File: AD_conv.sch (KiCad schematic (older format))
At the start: 30 parts, among them U9 74AHCT244

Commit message: 8-way buffer for ADC changed to 74ACT244PW second attempt
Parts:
- removed U9: 74AHCT244, symbol 74xx:74AHCT244
- added U9: 74ACT244PW, symbol OpenVent:74ACT244PW
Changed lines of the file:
@@
 $EndDescr
-$Comp
-L 74xx:74AHCT244 U9
-U 1 1 601B9EB9
-P 2650 2300
-F 0 "U9" H 2800 3100 50  0000 C CNN
-F 1 "74AHCT244" H 2950 3000 50  0000 C CNN
-F 2 "" H 2650 2300 50  0001 C CNN
-F 3 "https://assets.nexperia.com/documents/data-sheet/74AHC_AHCT244.pdf" H 2650 2300 50  0001 C CNN
-	1    2650 2300
-	1    0    0    -1
-$EndComp
 $Comp
 L OpenVent:100K_0603_Chip_Resistor,_1%,_0.1W R73
@@
 Wire Wire Line
 	4750 900  4950 900
+$Comp
+L OpenVent:74ACT244PW U9
+U 1 1 6054710B
+P 2650 2300
+F 0 "U9" H 2350 3100 50  0000 C CNN
+F 1 "74ACT244PW" H 2300 3000 50  0000 C CNN
+F 2 "" H 2650 2300 50  0001 C CNN
+F 3 "https://drive.google.com/drive/u/1/folders/1bT0MezjjDfDXdTdQktjf6O5y5oTJs8ND" H 2650 2300 50  0001 C CNN
+	1    2650 2300
+	1    0    0    -1
+$EndComp
 $EndSCHEMATC

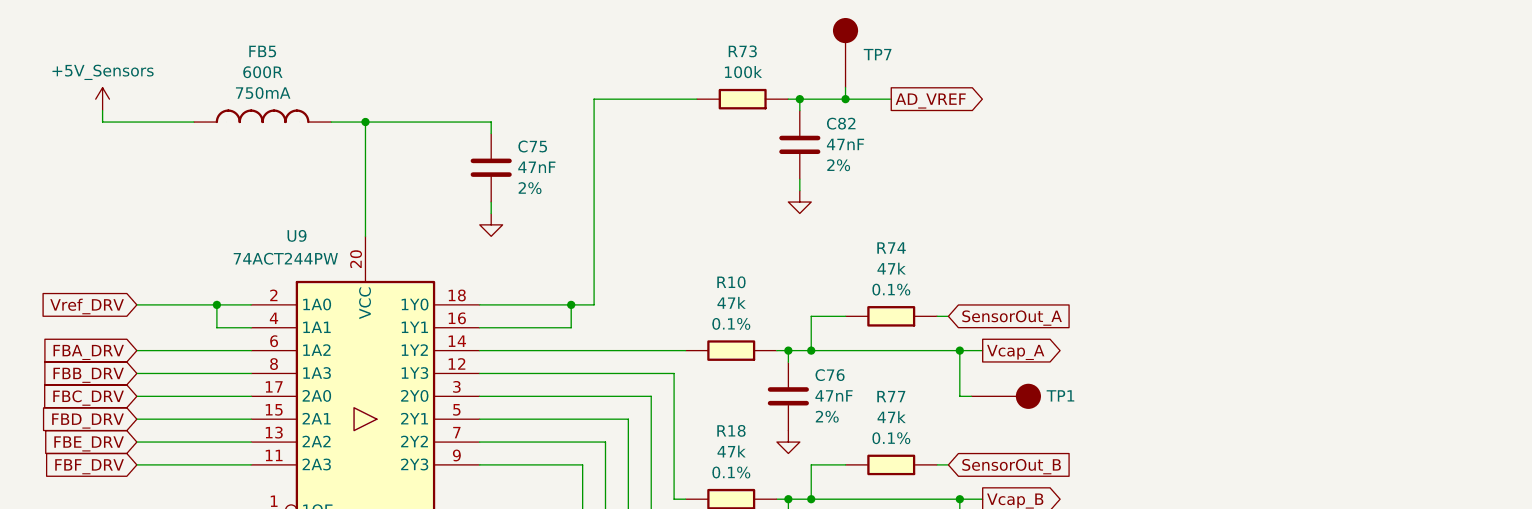
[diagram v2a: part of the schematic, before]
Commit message: Removed second Vref from U9 on ADC page, replaced with additional 8th input, G
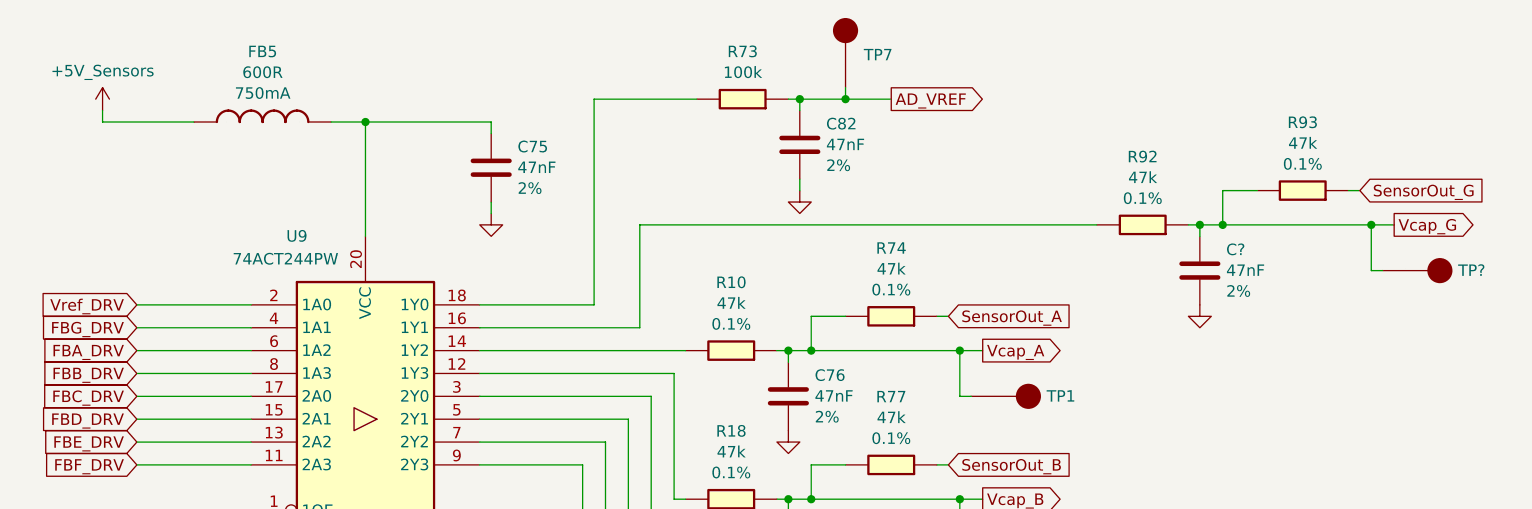
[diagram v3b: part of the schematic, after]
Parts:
- added C?: C_1206_47nF_16V_2%_PPS_film, Capacitor_SMD:C_1206_3216Metric, symbol OpenVent:C_1206_47nF_16V_2%_PPS_film
- added R92, R93: R_0603_47K_0.1%_0.1W_Film, Resistor_SMD:R_0603_1608Metric_Pad0.98x0.95mm_HandSolder, symbol OpenVent:R_0603_47K_0.1%_0.1W_Film
- added TP?: Test_Point_PTH, symbol OpenVent:Test_Point_PTH
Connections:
- net GND: now also C?.2
- net Vref_DRV: no longer U9.4 (1A1)
- net at R73.2, U9.18 (1Y0): no longer U9.16 (1Y1)
- new net: R92.2, U9.16 (1Y1)
- new net FBG_DRV: U9.4 (1A1)
- new net SensorOut_G: R93.1
- new net Vcap_G: C?.1, R92.1, R93.2, TP?.1
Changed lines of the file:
@@
 Text GLabel 1650 1800 0    50   Input ~ 0
 Vref_DRV
-Wire Wire Line
-	2150 1800 2000 1800
-Wire Wire Line
-	2150 1900 2000 1900
-Wire Wire Line
-	2000 1900 2000 1800
-Connection ~ 2000 1800
-Wire Wire Line
-	2000 1800 1650 1800
 Text GLabel 1650 2000 0    50   Input ~ 0
 FBA_DRV
@@
 $EndComp
 Wire Wire Line
-	3150 1800 3550 1800
-Wire Wire Line
 	3650 1800 3650 900
 Wire Wire Line
 	3650 900  4100 900
-Wire Wire Line
-	3150 1900 3550 1900
-Wire Wire Line
-	3550 1900 3550 1800
-Connection ~ 3550 1800
-Wire Wire Line
-	3550 1800 3650 1800
 Wire Wire Line
 	4500 900  4550 900
@@
 	1    0    0    -1
 $EndComp
+Wire Wire Line
+	1650 1800 2150 1800
+Wire Wire Line
+	3150 1800 3650 1800
+Text GLabel 1650 1900 0    50   Input ~ 0
+FBG_DRV
+Wire Wire Line
+	1650 1900 2150 1900
+$Comp
+L OpenVent:R_0603_47K_0.1%_0.1W_Film R92
+U 1 1 60565157
+P 6150 1550
+F 0 "R92" H 6250 1153 50  0000 C CNN
+F 1 "R_0603_47K_0.1%_0.1W_Film" H 6150 1550 50  0001 C CNN
+F 2 "Resistor_SMD:R_0603_1608Metric_Pad0.98x0.95mm_HandSolder" H 6150 1550 50  0001 C CNN
+F 3 "https://www.digikey.com/en/products/filter/chip-resistor-surface-mount/52" H 6150 1550 50  0001 C CNN
+F 4 "47k" H 6250 1244 50  0000 C CNN "Val"
+F 5 "0.1%" H 6250 1335 50  0000 C CNN "Tolerance"
+F 6 "0.1W" H 6150 1550 50  0001 C CNN "Watt"
+F 7 "KOA Speer Electronics, Inc." H 6150 1550 50  0001 C CNN "Mfr"
+F 8 "RN73H1JTTD4702B25" H 6150 1550 50  0001 C CNN "Mfr_PN"
+F 9 "RES 47K OHM 0.1% 1/10W 0603" H 6150 1550 50  0001 C CNN "Desc"
+F 10 "47 kOhms ±0.1% 0.1W, 1/10W Chip Resistor 0603 (1608 Metric) Automotive AEC-Q200, Moisture Resistant Metal Film" H 6150 1550 50  0001 C CNN "Detailed"
+	1    6150 1550
+	-1   0    0    1
+$EndComp
+$Comp
+L OpenVent:C_1206_47nF_16V_2%_PPS_film C?
+U 1 1 60565164
+P 6300 1650
+F 0 "C?" H 6415 1741 50  0000 L CNN
+F 1 "C_1206_47nF_16V_2%_PPS_film" H 6325 1550 50  0001 L CNN
+F 2 "Capacitor_SMD:C_1206_3216Metric" H 6338 1500 50  0001 C CNN
+F 3 "https://api.kemet.com/component-edge/download/datasheet/LDBAA2470GC5N0.pdf" H 6300 1650 50  0001 C CNN
+F 4 "Kemet" H 6300 1650 50  0001 C CNN "Mfr"
+F 5 "LDBAA2470GC5N0" H 6300 1650 50  0001 C CNN "Mfr_PN"
+F 6 "CAP FILM 0.047UF 2% 16VDC 1206" H 6300 1650 50  0001 C CNN "Desc"
+F 7 "0.047µF Film Capacitor  16V Polyphenylene Sulfide (PPS), Metallized - Stacked 1206 (3216 Metric)" H 6300 1650 50  0001 C CNN "Detailed"
+F 8 "47nF" H 6415 1650 50  0000 L CNN "Val"
+F 9 "2%" H 6415 1559 50  0000 L CNN "Tol"
+F 10 "16V" H 6300 1650 50  0001 C CNN "Volt"
+	1    6300 1650
+	1    0    0    -1
+$EndComp
+Wire Wire Line
+	6250 1450 6300 1450
+Wire Wire Line
+	6300 1450 6300 1500
+$Comp
+L OpenVent:GND #PWR?
+U 1 1 6056516C
+P 6300 1800
+F 0 "#PWR?" H 6300 1550 50  0001 C CNN
+F 1 "GND" H 6300 1650 50  0001 C CNN
+F 2 "" H 6300 1800 50  0001 C CNN
+F 3 "" H 6300 1800 50  0001 C CNN
+	1    6300 1800
+	1    0    0    -1
+$EndComp
+$Comp
+L OpenVent:R_0603_47K_0.1%_0.1W_Film R93
+U 1 1 60565179
+P 6850 1400
+F 0 "R93" H 6950 1003 50  0000 C CNN
+F 1 "R_0603_47K_0.1%_0.1W_Film" H 6850 1400 50  0001 C CNN
+F 2 "Resistor_SMD:R_0603_1608Metric_Pad0.98x0.95mm_HandSolder" H 6850 1400 50  0001 C CNN
+F 3 "https://www.digikey.com/en/products/filter/chip-resistor-surface-mount/52" H 6850 1400 50  0001 C CNN
+F 4 "47k" H 6950 1094 50  0000 C CNN "Val"
+F 5 "0.1%" H 6950 1185 50  0000 C CNN "Tolerance"
+F 6 "0.1W" H 6850 1400 50  0001 C CNN "Watt"
+F 7 "KOA Speer Electronics, Inc." H 6850 1400 50  0001 C CNN "Mfr"
+F 8 "RN73H1JTTD4702B25" H 6850 1400 50  0001 C CNN "Mfr_PN"
+F 9 "RES 47K OHM 0.1% 1/10W 0603" H 6850 1400 50  0001 C CNN "Desc"
+F 10 "47 kOhms ±0.1% 0.1W, 1/10W Chip Resistor 0603 (1608 Metric) Automotive AEC-Q200, Moisture Resistant Metal Film" H 6850 1400 50  0001 C CNN "Detailed"
+	1    6850 1400
+	-1   0    0    1
+$EndComp
+Text GLabel 7150 1450 2    50   Output ~ 0
+Vcap_G
+Wire Wire Line
+	6300 1450 6400 1450
+Connection ~ 6300 1450
+Wire Wire Line
+	6550 1300 6400 1300
+Wire Wire Line
+	6400 1300 6400 1450
+Connection ~ 6400 1450
+Wire Wire Line
+	6400 1450 7050 1450
+Text GLabel 7000 1300 2    50   Input ~ 0
+SensorOut_G
+Wire Wire Line
+	7000 1300 6950 1300
+$Comp
+L OpenVent:Test_Point_PTH TP?
+U 1 1 60565188
+P 7100 1650
+F 0 "TP?" H 6770 1650 50  0000 R CNN
+F 1 "Test_Point_PTH" H 7100 1650 50  0001 C CNN
+F 2 "" H 7100 1650 50  0001 C CNN
+F 3 "" H 7100 1650 50  0001 C CNN
+	1    7100 1650
+	-1   0    0    1
+$EndComp
+Wire Wire Line
+	7100 1650 7050 1650
+Wire Wire Line
+	7050 1650 7050 1450
+Connection ~ 7050 1450
+Wire Wire Line
+	7050 1450 7150 1450
+Wire Wire Line
+	5850 1450 3850 1450
+Wire Wire Line
+	3850 1450 3850 1900
+Wire Wire Line
+	3850 1900 3150 1900
 $EndSCHEMATC

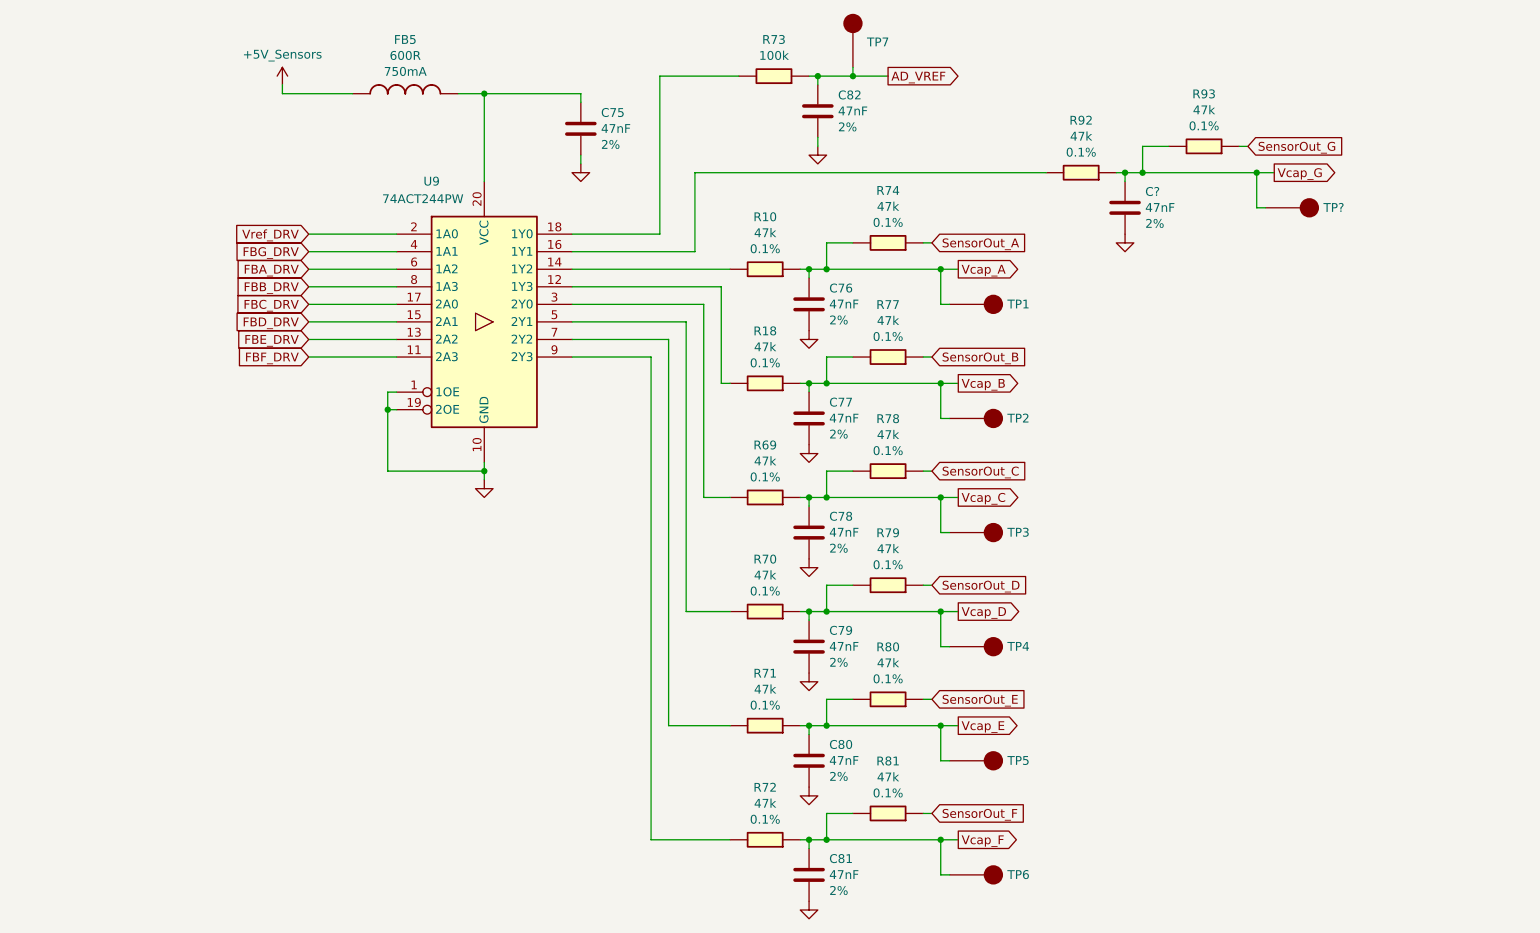
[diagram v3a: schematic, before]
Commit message: Removed attenuation from analogue sensor signals. Removed old ADC U13. Renamed sensor signal names on ADC sheet
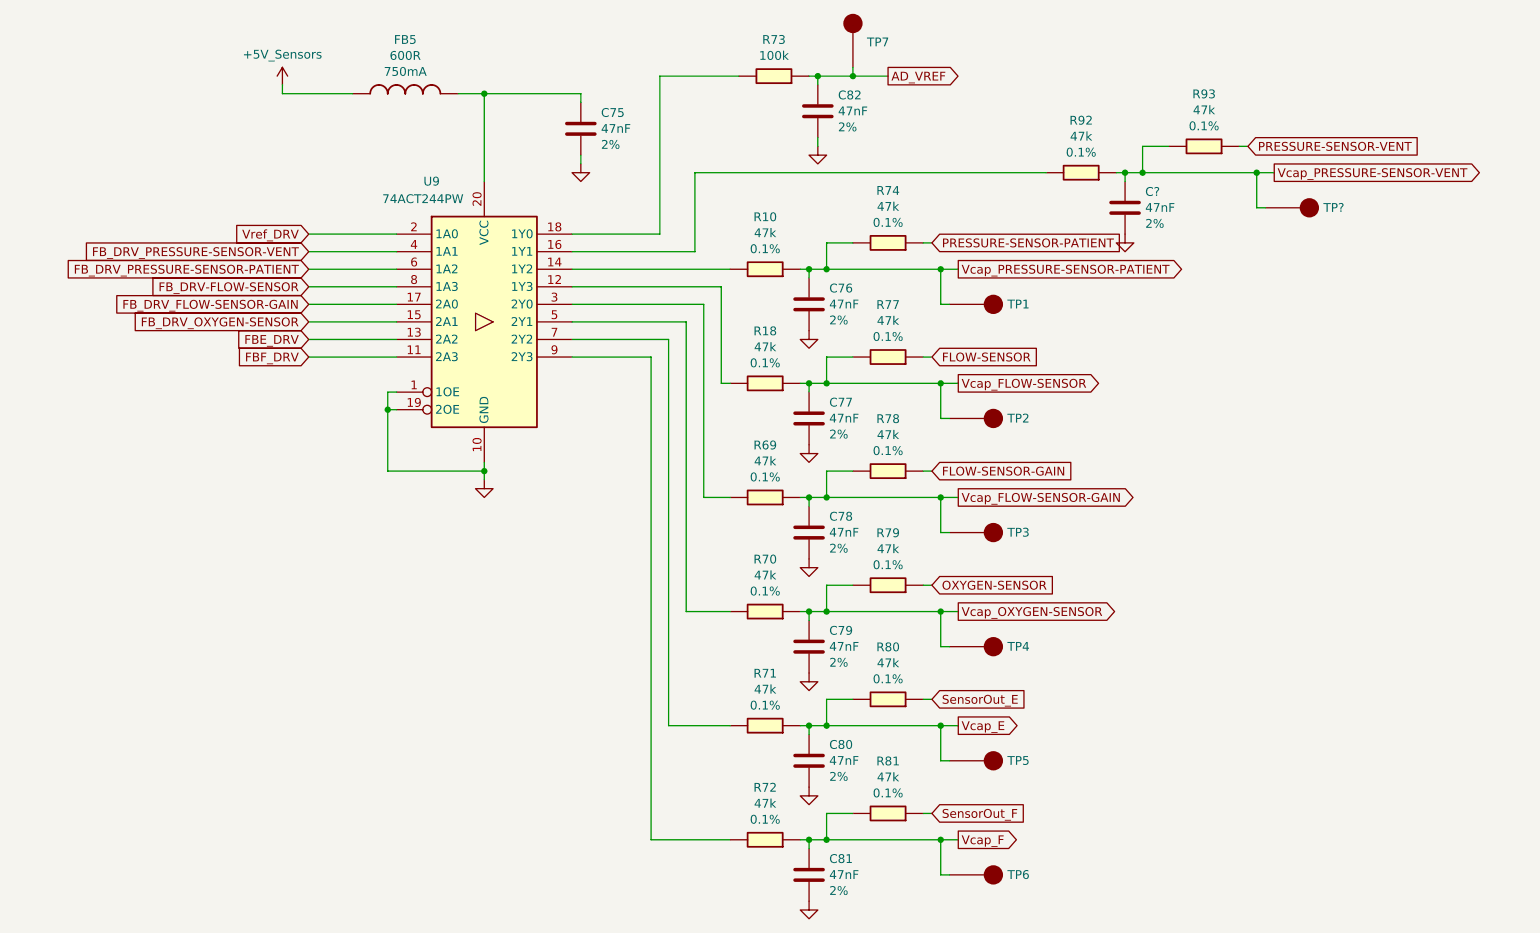
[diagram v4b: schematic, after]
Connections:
- net FBA_DRV renamed FB_DRV_PRESSURE-SENSOR-PATIENT
- net FBB_DRV renamed FB_DRV-FLOW-SENSOR
- net FBC_DRV renamed FB_DRV_FLOW-SENSOR-GAIN
- net FBD_DRV renamed FB_DRV_OXYGEN-SENSOR
- net FBG_DRV renamed FB_DRV_PRESSURE-SENSOR-VENT
- net SensorOut_A renamed PRESSURE-SENSOR-PATIENT
- net SensorOut_B renamed FLOW-SENSOR
- net SensorOut_C renamed FLOW-SENSOR-GAIN
- net SensorOut_D renamed OXYGEN-SENSOR
- net SensorOut_G renamed PRESSURE-SENSOR-VENT
- net Vcap_A renamed Vcap_PRESSURE-SENSOR-PATIENT
- net Vcap_B renamed Vcap_FLOW-SENSOR
- net Vcap_C renamed Vcap_FLOW-SENSOR-GAIN
- net Vcap_D renamed Vcap_OXYGEN-SENSOR
- net Vcap_G renamed Vcap_PRESSURE-SENSOR-VENT
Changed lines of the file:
@@
 Vref_DRV
 Text GLabel 1650 2000 0    50   Input ~ 0
-FBA_DRV
+FB_DRV_PRESSURE-SENSOR-PATIENT
 Text GLabel 1650 2100 0    50   Input ~ 0
-FBB_DRV
+FB_DRV-FLOW-SENSOR
 Text GLabel 1650 2200 0    50   Input ~ 0
-FBC_DRV
+FB_DRV_FLOW-SENSOR-GAIN
 Text GLabel 1650 2300 0    50   Input ~ 0
-FBD_DRV
+FB_DRV_OXYGEN-SENSOR
 Text GLabel 1650 2400 0    50   Input ~ 0
 FBE_DRV
@@
 $EndComp
 Text GLabel 5350 2000 2    50   Output ~ 0
-Vcap_A
+Vcap_PRESSURE-SENSOR-PATIENT
 Wire Wire Line
 	4500 2000 4600 2000
@@
 	4600 2000 5250 2000
 Text GLabel 5200 1850 2    50   Input ~ 0
-SensorOut_A
+PRESSURE-SENSOR-PATIENT
 Wire Wire Line
 	5200 1850 5150 1850
@@
 $EndComp
 Text GLabel 5350 2650 2    50   Output ~ 0
-Vcap_B
+Vcap_FLOW-SENSOR
 Wire Wire Line
 	4500 2650 4600 2650
@@
 	4600 2650 5250 2650
 Text GLabel 5200 2500 2    50   Input ~ 0
-SensorOut_B
+FLOW-SENSOR
 Wire Wire Line
 	5200 2500 5150 2500
@@
 $EndComp
 Text GLabel 5350 3300 2    50   Output ~ 0
-Vcap_C
+Vcap_FLOW-SENSOR-GAIN
 Wire Wire Line
 	4500 3300 4600 3300
@@
 	4600 3300 5250 3300
 Text GLabel 5200 3150 2    50   Input ~ 0
-SensorOut_C
+FLOW-SENSOR-GAIN
 Wire Wire Line
 	5200 3150 5150 3150
@@
 $EndComp
 Text GLabel 5350 3950 2    50   Output ~ 0
-Vcap_D
+Vcap_OXYGEN-SENSOR
 Wire Wire Line
 	4500 3950 4600 3950
@@
 	4600 3950 5250 3950
 Text GLabel 5200 3800 2    50   Input ~ 0
-SensorOut_D
+OXYGEN-SENSOR
 Wire Wire Line
 	5200 3800 5150 3800
@@
 	3150 1800 3650 1800
 Text GLabel 1650 1900 0    50   Input ~ 0
-FBG_DRV
+FB_DRV_PRESSURE-SENSOR-VENT
 Wire Wire Line
 	1650 1900 2150 1900
@@
 $EndComp
 Text GLabel 7150 1450 2    50   Output ~ 0
-Vcap_G
+Vcap_PRESSURE-SENSOR-VENT
 Wire Wire Line
 	6300 1450 6400 1450
@@
 	6400 1450 7050 1450
 Text GLabel 7000 1300 2    50   Input ~ 0
-SensorOut_G
+PRESSURE-SENSOR-VENT
 Wire Wire Line
 	7000 1300 6950 1300
